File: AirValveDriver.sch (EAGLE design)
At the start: 16 parts, among them IC2 NE555, Q1 2N2222, Q2 STF40NF06

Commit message: updated after DRC
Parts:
- C1: device resistor:C-US025-030X050 -> myDevices:CAPACITOR_POLARIZED
- C2, C4: value 10u -> CAPACITOR_POLARIZED; device resistor:C-US025-030X050 -> myDevices:CAPACITOR_POLARIZED
- C3: value 0.1u -> CAPACITOR_POLARIZED; device resistor:C-US025-030X050 -> myDevices:CAPACITOR_POLARIZED
- IC1: value (none) -> LM7805
- Q1: device transistor-npn:2N2222 -> myDevices:2N2222
- R1, R2, R3, R4, R5: device resistor:R-US_0207/10 -> myDevices:RESISTOR
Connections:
- net +5V: now also C4.+; no longer C4.1
- net AGND: now also C2.-, C3.-, C4.-, R2.1; no longer C2.2, C3.2, C4.2, R2.2
- net N$1: now also C3.+; no longer C3.1
- net N$10: now also C2.+; no longer C2.1
- net N$5: now also C1.+; no longer C1.1
- net N$6: now also C1.-, R2.2; no longer C1.2, R2.1
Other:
- moved on the sheet: R2, R5

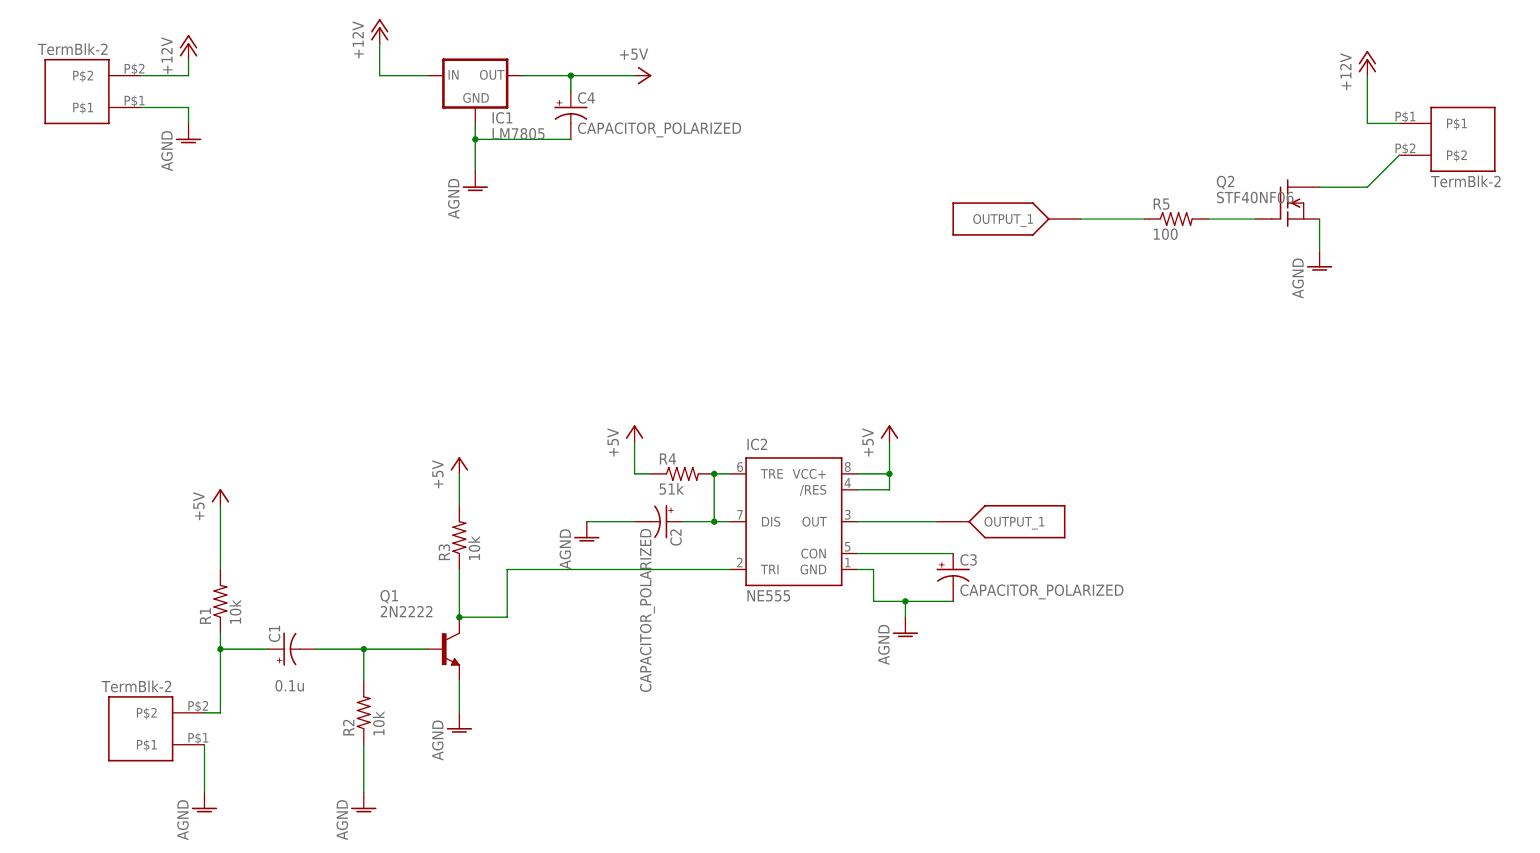
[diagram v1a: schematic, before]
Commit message: mod board to use compliant drills
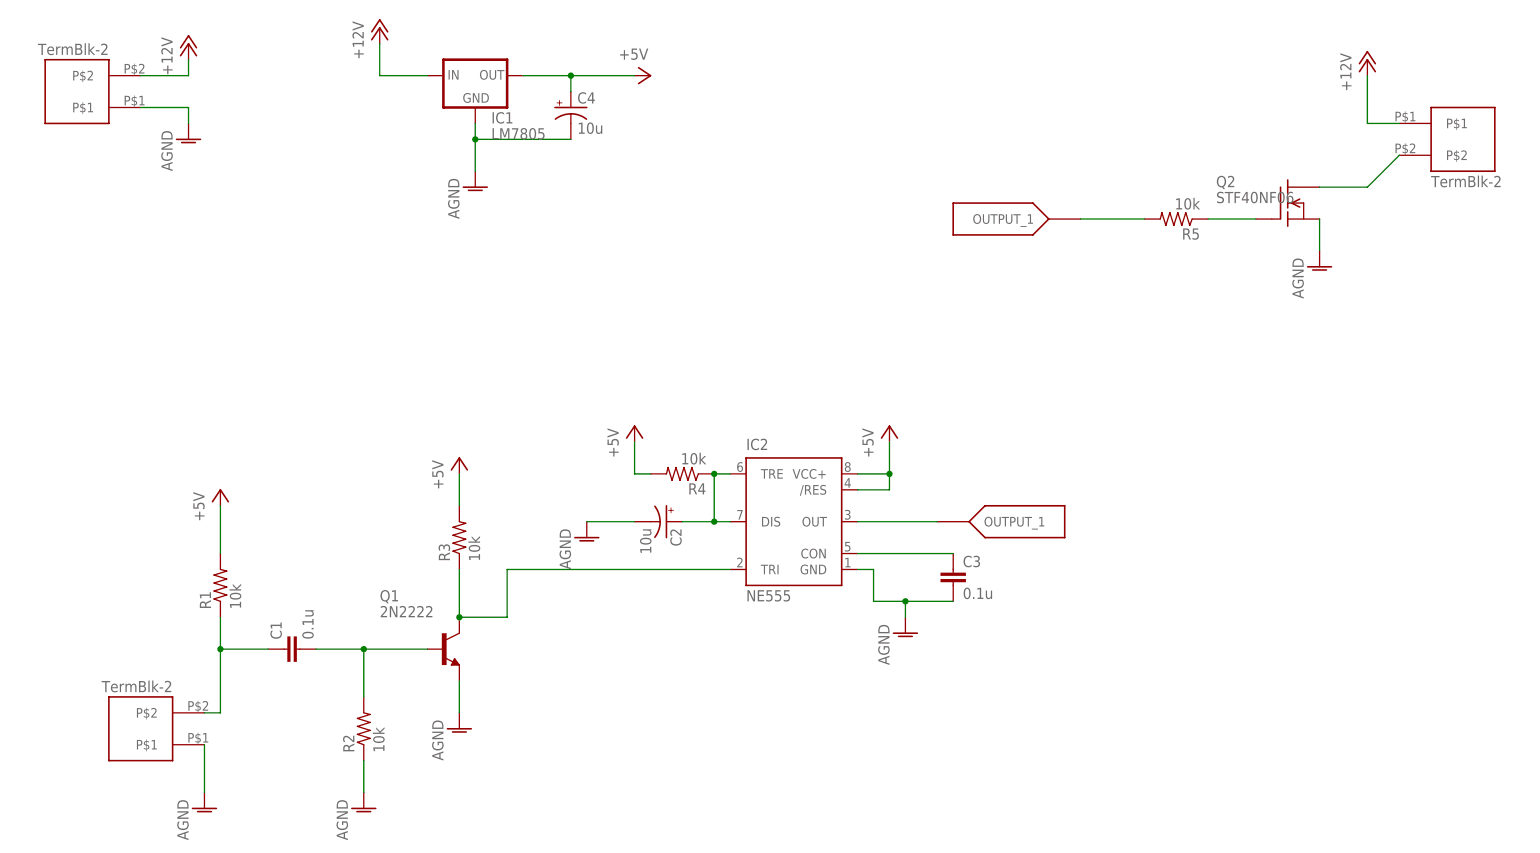
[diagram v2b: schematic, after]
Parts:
- removed POWER_IN: PWR_IN, myLibrary:TB2
- added U$5: TB2, myDevices:TB2
- C1: device myDevices:CAPACITOR_POLARIZED -> myDevices:CAPACITOR_CERAMIC
- C2, C4: value CAPACITOR_POLARIZED -> 10u
- C3: value CAPACITOR_POLARIZED -> 0.1u; device myDevices:CAPACITOR_POLARIZED -> myDevices:CAPACITOR_CERAMIC
- R4: value 51k -> 10k
- R5: value 100 -> 10k
- U$2: value Air Valve -> TB2; device myLibrary:TB2 -> myDevices:TB2
- U$3: value switch -> Pwr; device myLibrary:TB2 -> myDevices:TB2
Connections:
- net +12V: now also U$3.P$2; no longer POWER_IN.P$2
- net +5V: now also R4.2; no longer R4.1
- net AGND: now also C3.2, U$5.P$1; no longer C3.-, POWER_IN.P$1
- net N$1: now also C3.1; no longer C3.+
- net N$10: now also R4.1; no longer R4.2
- net N$2: now also R5.1; no longer R5.2
- net N$5: now also C1.1, U$5.P$2; no longer C1.+, U$3.P$2
- net N$6: now also C1.2; no longer C1.-
- net OUTPUT_1: now also R5.2; no longer R5.1
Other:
- moved on the sheet: R1, R2, R4, R5
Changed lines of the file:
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@@
 <part name="Q2" library="transistor-fet" deviceset="IRF540" device="" value="STF40NF06"/>
 <part name="IC2" library="st-microelectronics" deviceset="NE555" device=""/>
-<part name="POWER_IN" library="myLibrary" deviceset="TB2" device="" value="PWR_IN"/>
-<part name="U$2" library="myLibrary" deviceset="TB2" device="" value="Air Valve"/>
-<part name="U$3" library="myLibrary" deviceset="TB2" device="" value="switch"/>
 <part name="U$1" library="myLibrary" deviceset="OUTPUT_1" device=""/>
 <part name="U$4" library="myLibrary" deviceset="OUTPUT_1" device=""/>
-<part name="C4" library="myDevices" deviceset="CAPACITOR_POLARIZED" device=""/>
-<part name="C1" library="myDevices" deviceset="CAPACITOR_POLARIZED" device="" value="0.1u"/>
-<part name="C2" library="myDevices" deviceset="CAPACITOR_POLARIZED" device=""/>
-<part name="C3" library="myDevices" deviceset="CAPACITOR_POLARIZED" device=""/>
 <part name="Q1" library="myDevices" deviceset="2N2222*" device=""/>
 <part name="R1" library="myDevices" deviceset="RESISTOR" device="" value="10k"/>
 <part name="R2" library="myDevices" deviceset="RESISTOR" device="" value="10k"/>
 <part name="R3" library="myDevices" deviceset="RESISTOR" device="" value="10k"/>
-<part name="R4" library="myDevices" deviceset="RESISTOR" device="" value="51k"/>
-<part name="R5" library="myDevices" deviceset="RESISTOR" device="" value="100"/>
+<part name="R4" library="myDevices" deviceset="RESISTOR" device="" value="10k"/>
+<part name="R5" library="myDevices" deviceset="RESISTOR" device="" value="10k"/>
+<part name="C1" library="myDevices" deviceset="CAPACITOR_CERAMIC" device="" value="0.1u"/>
+<part name="C3" library="myDevices" deviceset="CAPACITOR_CERAMIC" device="" value="0.1u"/>
+<part name="C2" library="myDevices" deviceset="CAPACITOR_POLARIZED" device="" value="10u"/>
+<part name="C4" library="myDevices" deviceset="CAPACITOR_POLARIZED" device="" value="10u"/>
+<part name="U$3" library="myDevices" deviceset="TB2" device="" value="Pwr"/>
+<part name="U$5" library="myDevices" deviceset="TB2" device=""/>
+<part name="U$2" library="myDevices" deviceset="TB2" device=""/>
 </parts>
 <sheets>
@@
 <instance part="Q2" gate="G$1" x="210.82" y="134.62"/>
 <instance part="IC2" gate="G$1" x="132.08" y="83.82"/>
-<instance part="POWER_IN" gate="G$1" x="22.86" y="152.4" rot="R180"/>
-<instance part="U$2" gate="G$1" x="233.68" y="144.78"/>
-<instance part="U$3" gate="G$1" x="33.02" y="50.8" rot="R180"/>
 <instance part="U$1" gate="G$1" x="160.02" y="83.82"/>
 <instance part="U$4" gate="G$1" x="172.72" y="132.08" rot="R180"/>
+<instance part="Q1" gate="G$1" x="76.2" y="63.5"/>
+<instance part="R1" gate="G$1" x="40.64" y="73.66" rot="R90"/>
+<instance part="R2" gate="G$1" x="63.5" y="50.8" rot="R90"/>
+<instance part="R3" gate="G$1" x="78.74" y="81.28" rot="R90"/>
+<instance part="R4" gate="G$1" x="114.3" y="91.44" rot="R180"/>
+<instance part="R5" gate="G$1" x="193.04" y="132.08" rot="R180"/>
+<instance part="C1" gate="G$1" x="53.34" y="63.5" rot="R90"/>
+<instance part="C3" gate="G$1" x="157.48" y="73.66"/>
+<instance part="C2" gate="G$1" x="111.76" y="83.82" rot="R270"/>
 <instance part="C4" gate="G$1" x="96.52" y="149.86"/>
-<instance part="C1" gate="G$1" x="50.8" y="63.5" smashed="yes" rot="R90">
-<attribute name="NAME" x="50.165" y="64.516" size="1.778" layer="95" rot="R90"/>
-<attribute name="VALUE" x="49.276" y="56.769" size="1.778" layer="96"/>
-</instance>
-<instance part="C2" gate="G$1" x="111.76" y="83.82" rot="R270"/>
-<instance part="C3" gate="G$1" x="157.48" y="76.2"/>
-<instance part="Q1" gate="G$1" x="76.2" y="63.5"/>
-<instance part="R1" gate="G$1" x="40.64" y="71.12" rot="R90"/>
-<instance part="R2" gate="G$1" x="63.5" y="53.34" rot="R90"/>
-<instance part="R3" gate="G$1" x="78.74" y="81.28" rot="R90"/>
-<instance part="R4" gate="G$1" x="114.3" y="91.44"/>
-<instance part="R5" gate="G$1" x="193.04" y="132.08"/>
+<instance part="U$3" gate="G$1" x="22.86" y="152.4" rot="R180"/>
+<instance part="U$5" gate="G$1" x="33.02" y="50.8" rot="R180"/>
+<instance part="U$2" gate="G$1" x="233.68" y="144.78"/>
 </instances>
 <busses>
@@
 <net name="+12V" class="0">
 <segment>
-<pinref part="POWER_IN" gate="G$1" pin="P$2"/>
 <wire x1="27.94" y1="154.94" x2="35.56" y2="154.94" width="0.1524" layer="91"/>
 <pinref part="P+9" gate="1" pin="+12V"/>
 <wire x1="35.56" y1="154.94" x2="35.56" y2="157.48" width="0.1524" layer="91"/>
+<pinref part="U$3" gate="G$1" pin="P$2"/>
 </segment>
 <segment>
@@
 <pinref part="P+8" gate="1" pin="+12V"/>
 <wire x1="223.52" y1="154.94" x2="223.52" y2="147.32" width="0.1524" layer="91"/>
+<wire x1="223.52" y1="147.32" x2="228.6" y2="147.32" width="0.1524" layer="91"/>
 <pinref part="U$2" gate="G$1" pin="P$1"/>
-<wire x1="223.52" y1="147.32" x2="228.6" y2="147.32" width="0.1524" layer="91"/>
 </segment>
 </net>
 <net name="AGND" class="0">
 <segment>
-<pinref part="POWER_IN" gate="G$1" pin="P$1"/>
 <wire x1="27.94" y1="149.86" x2="35.56" y2="149.86" width="0.1524" layer="91"/>
 <pinref part="AGND10" gate="VR1" pin="AGND"/>
 <wire x1="35.56" y1="149.86" x2="35.56" y2="147.32" width="0.1524" layer="91"/>
+<pinref part="U$3" gate="G$1" pin="P$1"/>
 </segment>
 <segment>
@@
 <pinref part="IC1" gate="A" pin="GND"/>
 <wire x1="81.28" y1="147.32" x2="81.28" y2="144.78" width="0.1524" layer="91"/>
-<pinref part="C4" gate="G$1" pin="-"/>
 <wire x1="81.28" y1="144.78" x2="81.28" y2="139.7" width="0.1524" layer="91"/>
 <wire x1="96.52" y1="144.78" x2="81.28" y2="144.78" width="0.1524" layer="91"/>
 <junction x="81.28" y="144.78"/>
-</segment>
-<segment>
-<pinref part="U$3" gate="G$1" pin="P$1"/>
+<pinref part="C4" gate="G$1" pin="-"/>
+</segment>
+<segment>
 <pinref part="AGND5" gate="VR1" pin="AGND"/>
 <wire x1="38.1" y1="48.26" x2="38.1" y2="40.64" width="0.1524" layer="91"/>
+<pinref part="U$5" gate="G$1" pin="P$1"/>
 </segment>
 <segment>
 <pinref part="AGND6" gate="VR1" pin="AGND"/>
-<wire x1="63.5" y1="48.26" x2="63.5" y2="40.64" width="0.1524" layer="91"/>
+<wire x1="63.5" y1="45.72" x2="63.5" y2="40.64" width="0.1524" layer="91"/>
 <pinref part="R2" gate="G$1" pin="1"/>
 </segment>
@@
 <wire x1="149.86" y1="68.58" x2="149.86" y2="71.12" width="0.1524" layer="91"/>
 <junction x="149.86" y="71.12"/>
-<pinref part="C3" gate="G$1" pin="-"/>
+<pinref part="C3" gate="G$1" pin="2"/>
 </segment>
 <segment>
@@
 <segment>
 <pinref part="P+2" gate="1" pin="+5V"/>
-<wire x1="40.64" y1="86.36" x2="40.64" y2="76.2" width="0.1524" layer="91"/>
+<wire x1="40.64" y1="86.36" x2="40.64" y2="78.74" width="0.1524" layer="91"/>
 <pinref part="R1" gate="G$1" pin="2"/>
 </segment>
@@
 <pinref part="P+3" gate="1" pin="+5V"/>
 <wire x1="106.68" y1="91.44" x2="106.68" y2="96.52" width="0.1524" layer="91"/>
-<pinref part="R4" gate="G$1" pin="1"/>
+<pinref part="R4" gate="G$1" pin="2"/>
 </segment>
 <segment>
@@
 <pinref part="P+1" gate="1" pin="+5V"/>
 <wire x1="88.9" y1="154.94" x2="96.52" y2="154.94" width="0.1524" layer="91"/>
-<pinref part="C4" gate="G$1" pin="+"/>
 <wire x1="96.52" y1="154.94" x2="106.68" y2="154.94" width="0.1524" layer="91"/>
 <wire x1="96.52" y1="152.4" x2="96.52" y2="154.94" width="0.1524" layer="91"/>
 <junction x="96.52" y="154.94"/>
+<pinref part="C4" gate="G$1" pin="+"/>
 </segment>
 </net>
 <net name="N$5" class="0">
 <segment>
-<pinref part="U$3" gate="G$1" pin="P$2"/>
-<wire x1="40.64" y1="66.04" x2="40.64" y2="63.5" width="0.1524" layer="91"/>
+<wire x1="40.64" y1="68.58" x2="40.64" y2="63.5" width="0.1524" layer="91"/>
 <wire x1="40.64" y1="63.5" x2="40.64" y2="53.34" width="0.1524" layer="91"/>
 <wire x1="40.64" y1="53.34" x2="38.1" y2="53.34" width="0.1524" layer="91"/>
-<pinref part="C1" gate="G$1" pin="+"/>
 <wire x1="48.26" y1="63.5" x2="40.64" y2="63.5" width="0.1524" layer="91"/>
 <junction x="40.64" y="63.5"/>
 <pinref part="R1" gate="G$1" pin="1"/>
+<pinref part="C1" gate="G$1" pin="1"/>
+<pinref part="U$5" gate="G$1" pin="P$2"/>
 </segment>
 </net>
@@
 <segment>
 <wire x1="63.5" y1="63.5" x2="73.66" y2="63.5" width="0.1524" layer="91"/>
-<wire x1="63.5" y1="58.42" x2="63.5" y2="63.5" width="0.1524" layer="91"/>
-<pinref part="C1" gate="G$1" pin="-"/>
+<wire x1="63.5" y1="55.88" x2="63.5" y2="63.5" width="0.1524" layer="91"/>
 <wire x1="55.88" y1="63.5" x2="63.5" y2="63.5" width="0.1524" layer="91"/>
 <junction x="63.5" y="63.5"/>
 <pinref part="Q1" gate="G$1" pin="B"/>
 <pinref part="R2" gate="G$1" pin="2"/>
+<pinref part="C1" gate="G$1" pin="2"/>
 </segment>
 </net>
@@
 <wire x1="114.3" y1="83.82" x2="119.38" y2="83.82" width="0.1524" layer="91"/>
 <junction x="119.38" y="83.82"/>
+<pinref part="R4" gate="G$1" pin="1"/>
+<junction x="119.38" y="91.44"/>
 <pinref part="C2" gate="G$1" pin="+"/>
-<pinref part="R4" gate="G$1" pin="2"/>
-<junction x="119.38" y="91.44"/>
 </segment>
 </net>
@@
 <pinref part="IC2" gate="G$1" pin="CON"/>
 <wire x1="142.24" y1="78.74" x2="157.48" y2="78.74" width="0.1524" layer="91"/>
-<pinref part="C3" gate="G$1" pin="+"/>
+<pinref part="C3" gate="G$1" pin="1"/>
 </segment>
 </net>
@@
 </segment>
 <segment>
-<pinref part="R5" gate="G$1" pin="1"/>
 <pinref part="U$4" gate="G$1" pin="OUTPUT_1"/>
 <wire x1="187.96" y1="132.08" x2="177.8" y2="132.08" width="0.1524" layer="91"/>
+<pinref part="R5" gate="G$1" pin="2"/>
 </segment>
 </net>
@@
 <pinref part="Q2" gate="G$1" pin="D"/>
 <wire x1="215.9" y1="137.16" x2="223.52" y2="137.16" width="0.1524" layer="91"/>
+<wire x1="223.52" y1="137.16" x2="228.6" y2="142.24" width="0.1524" layer="91"/>
 <pinref part="U$2" gate="G$1" pin="P$2"/>
-<wire x1="223.52" y1="137.16" x2="228.6" y2="142.24" width="0.1524" layer="91"/>
 </segment>
 </net>
 <net name="N$2" class="0">
 <segment>
-<pinref part="R5" gate="G$1" pin="2"/>
 <pinref part="Q2" gate="G$1" pin="G"/>
 <wire x1="198.12" y1="132.08" x2="205.74" y2="132.08" width="0.1524" layer="91"/>
-</segment>
-</net>
+<pinref part="R5" gate="G$1" pin="1"/>
+</segment>
+</net>

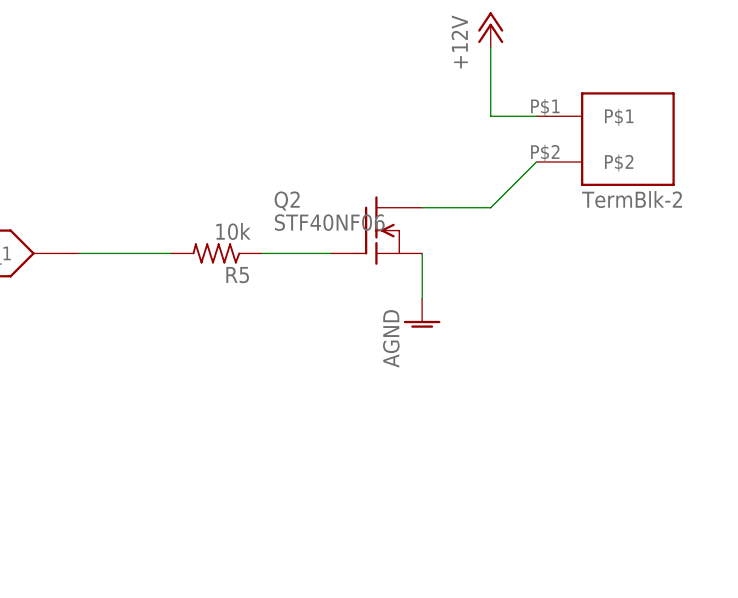
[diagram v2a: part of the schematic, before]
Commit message: updated cam files to run a copy of the board
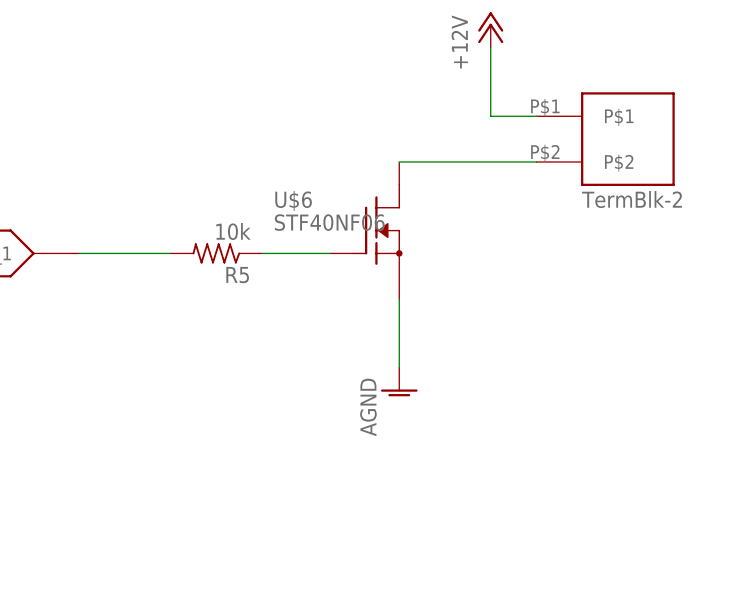
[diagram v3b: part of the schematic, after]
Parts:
- removed Q2: STF40NF06, transistor-fet:IRF540
- added U$6: STF40NF06, myDevices:STF40NF06
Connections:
- removed net N$4: Q2.D, U$2.P$2
- new net N$3: U$2.P$2, U$6.D
- net AGND: now also U$6.S; no longer Q2.S
- net N$2: now also U$6.G; no longer Q2.G
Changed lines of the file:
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@@
 <part name="P+9" library="supply1" deviceset="+12V" device=""/>
 <part name="IC1" library="v-reg" deviceset="78XXL" device="" value="LM7805"/>
-<part name="Q2" library="transistor-fet" deviceset="IRF540" device="" value="STF40NF06"/>
 <part name="IC2" library="st-microelectronics" deviceset="NE555" device=""/>
 <part name="U$1" library="myLibrary" deviceset="OUTPUT_1" device=""/>
@@
 <part name="U$5" library="myDevices" deviceset="TB2" device=""/>
 <part name="U$2" library="myDevices" deviceset="TB2" device=""/>
+<part name="U$6" library="myDevices" deviceset="STF40NF06" device=""/>
 </parts>
 <sheets>
@@
 <instance part="AGND6" gate="VR1" x="63.5" y="38.1"/>
 <instance part="AGND7" gate="VR1" x="99.06" y="81.28"/>
-<instance part="AGND8" gate="VR1" x="215.9" y="124.46"/>
+<instance part="AGND8" gate="VR1" x="213.36" y="116.84"/>
 <instance part="AGND9" gate="VR1" x="81.28" y="137.16"/>
 <instance part="AGND10" gate="VR1" x="35.56" y="144.78"/>
@@
 <instance part="P+9" gate="1" x="35.56" y="160.02"/>
 <instance part="IC1" gate="A" x="81.28" y="154.94"/>
-<instance part="Q2" gate="G$1" x="210.82" y="134.62"/>
 <instance part="IC2" gate="G$1" x="132.08" y="83.82"/>
 <instance part="U$1" gate="G$1" x="160.02" y="83.82"/>
@@
 <instance part="U$5" gate="G$1" x="33.02" y="50.8" rot="R180"/>
 <instance part="U$2" gate="G$1" x="233.68" y="144.78"/>
+<instance part="U$6" gate="G$1" x="210.82" y="134.62"/>
 </instances>
 <busses>
@@
 </segment>
 <segment>
-<pinref part="Q2" gate="G$1" pin="S"/>
+<pinref part="U$6" gate="G$1" pin="S"/>
 <pinref part="AGND8" gate="VR1" pin="AGND"/>
-<wire x1="215.9" y1="132.08" x2="215.9" y2="127" width="0.1524" layer="91"/>
+<wire x1="213.36" y1="127" x2="213.36" y2="119.38" width="0.1524" layer="91"/>
 </segment>
 </net>
@@
 </segment>
 </net>
-<net name="N$4" class="0">
-<segment>
-<pinref part="Q2" gate="G$1" pin="D"/>
-<wire x1="215.9" y1="137.16" x2="223.52" y2="137.16" width="0.1524" layer="91"/>
-<wire x1="223.52" y1="137.16" x2="228.6" y2="142.24" width="0.1524" layer="91"/>
-<pinref part="U$2" gate="G$1" pin="P$2"/>
-</segment>
-</net>
 <net name="N$2" class="0">
 <segment>
-<pinref part="Q2" gate="G$1" pin="G"/>
 <wire x1="198.12" y1="132.08" x2="205.74" y2="132.08" width="0.1524" layer="91"/>
 <pinref part="R5" gate="G$1" pin="1"/>
-</segment>
-</net>
+<pinref part="U$6" gate="G$1" pin="G"/>
+</segment>
+</net>
+<net name="N$3" class="0">
+<segment>
+<pinref part="U$6" gate="G$1" pin="D"/>
+<pinref part="U$2" gate="G$1" pin="P$2"/>
+<wire x1="213.36" y1="142.24" x2="228.6" y2="142.24" width="0.1524" layer="91"/>
+</segment>
+</net>
